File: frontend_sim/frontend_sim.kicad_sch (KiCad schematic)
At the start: 15 parts, among them U1 TL072

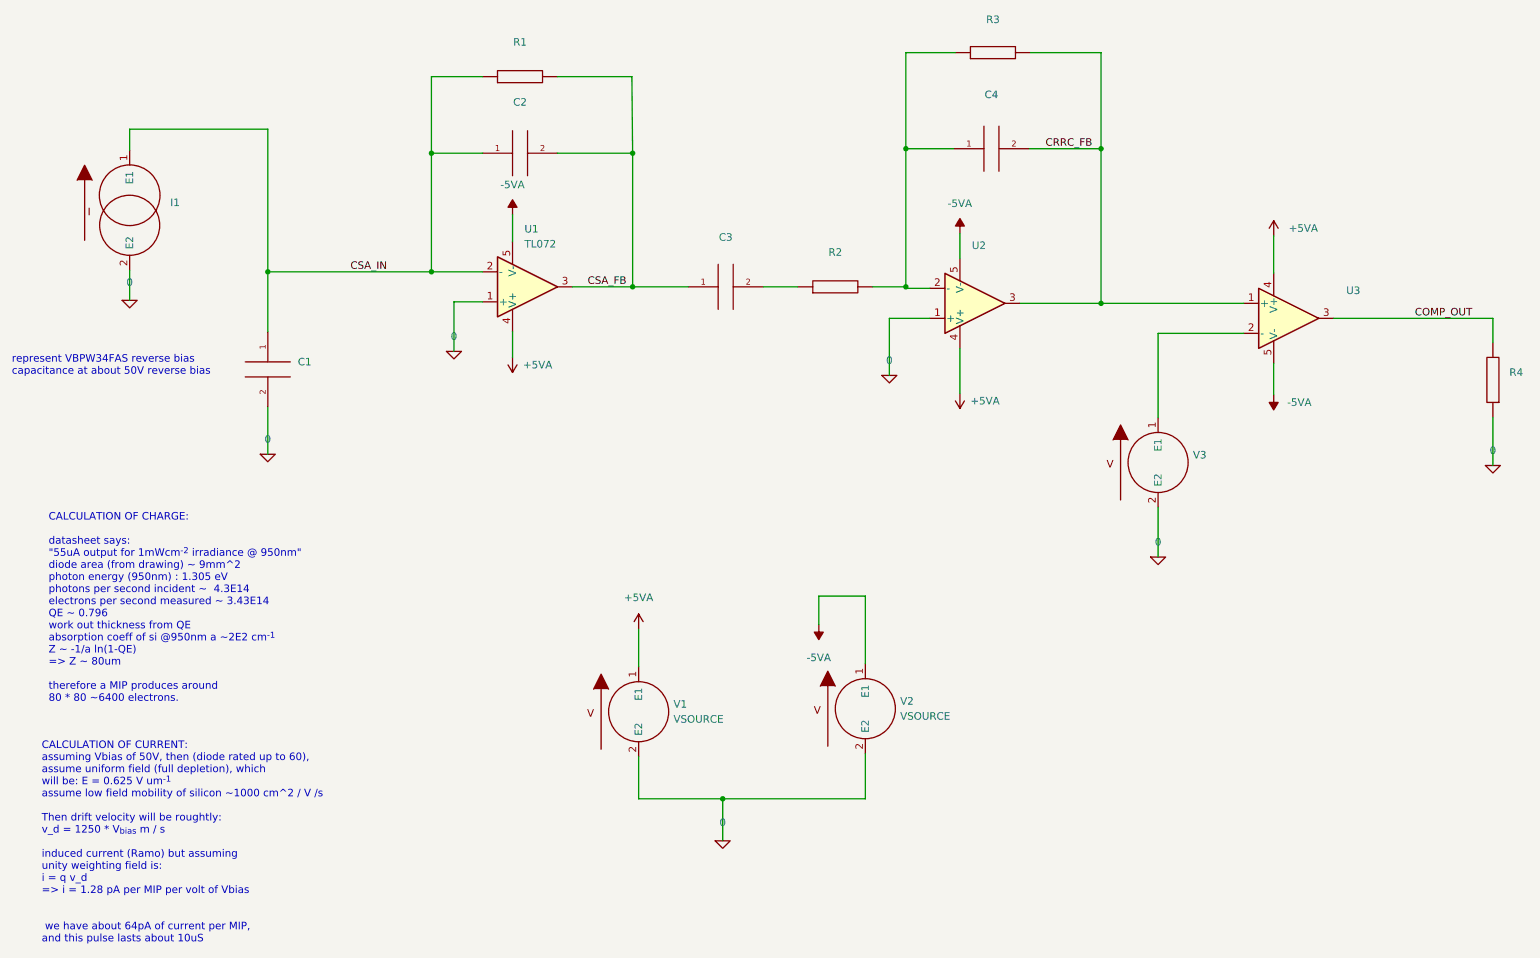
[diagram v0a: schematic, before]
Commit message: frontend sim update to v8, working at least AC scan mode
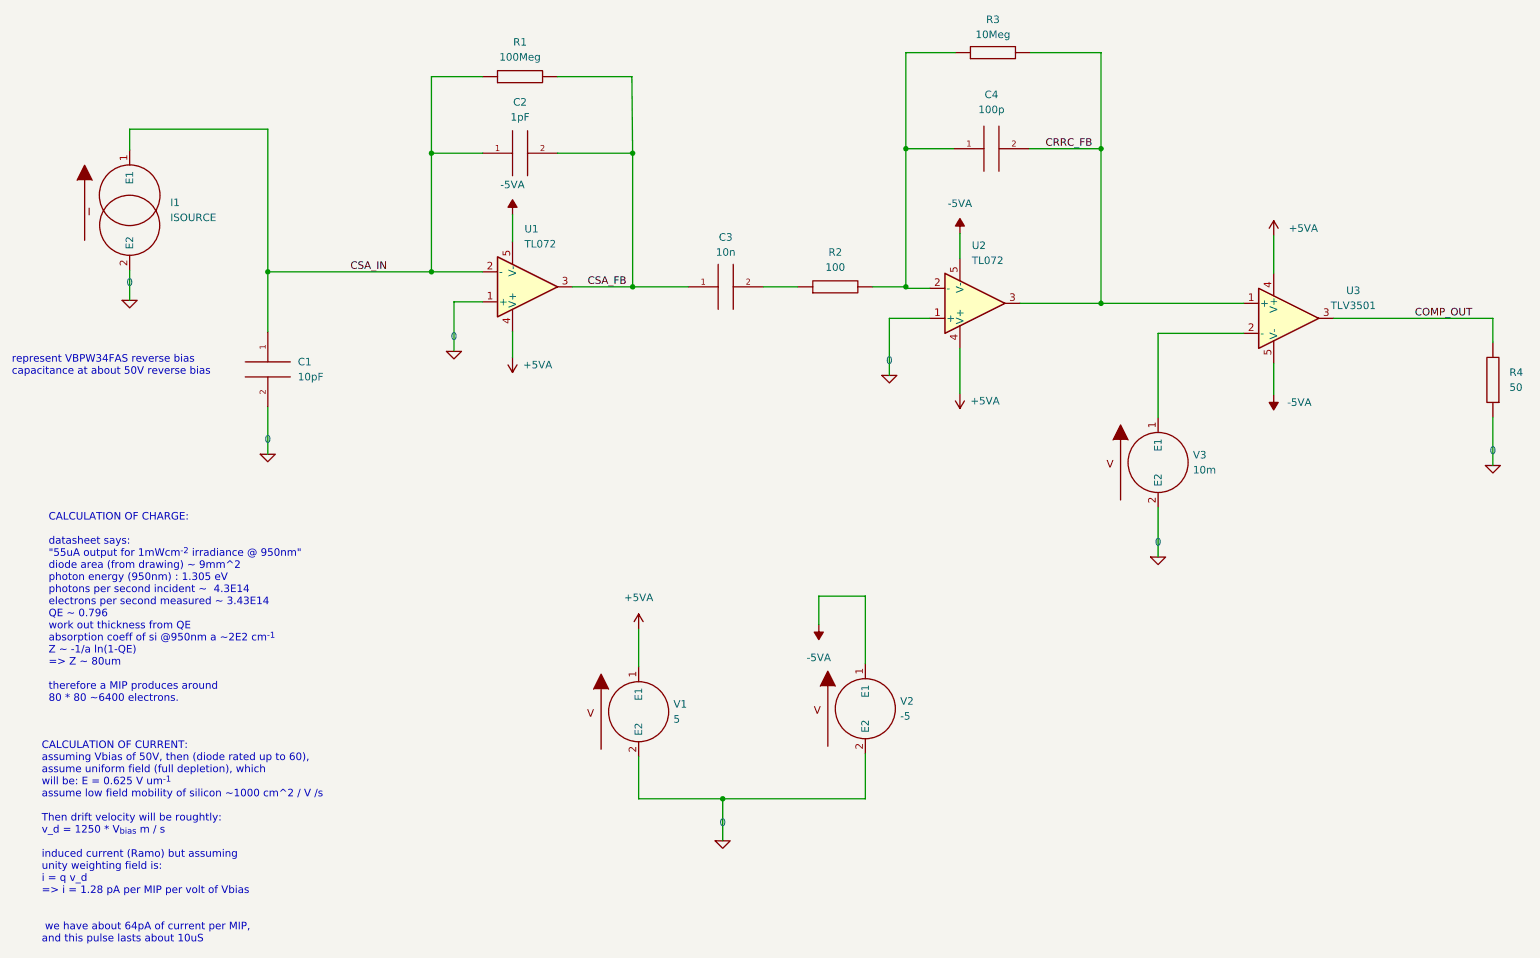
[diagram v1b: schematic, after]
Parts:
- C1: value (none) -> 10pF
- C2: value (none) -> 1pF; Spice_Model 2p -> (none); Spice_Netlist_Enabled Y -> (none); Spice_Primitive C -> (none)
- C3: value (none) -> 10n; Spice_Model 10n -> (none); Spice_Netlist_Enabled Y -> (none); Spice_Primitive C -> (none)
- C4: value (none) -> 100p; Spice_Model 10p -> (none); Spice_Netlist_Enabled Y -> (none); Spice_Primitive C -> (none)
- I1: value (none) -> ISOURCE; Spice_Model dc 0 ac 10n pulse(0 -100p 1n 100p 100p 1u) -> (none); Spice_Netlist_Enabled Y -> (none); Spice_Primitive I -> (none)
- R1: value (none) -> 100Meg; Spice_Model 100Meg -> (none); Spice_Netlist_Enabled Y -> (none); Spice_Primitive R -> (none)
- R2: value (none) -> 100; Spice_Model 100 -> (none); Spice_Netlist_Enabled Y -> (none); Spice_Primitive R -> (none)
- R3: value (none) -> 10Meg; Spice_Model 100Meg -> (none); Spice_Netlist_Enabled Y -> (none); Spice_Primitive R -> (none)
- R4: value (none) -> 50; Spice_Model 50 -> (none); Spice_Netlist_Enabled Y -> (none); Spice_Primitive R -> (none)
- U1: Spice_Lib_File TL072.301 -> (none); Spice_Model TL072 -> (none); Spice_Netlist_Enabled Y -> (none); Spice_Node_Sequence 1 2 4 5 3 -> (none); Spice_Primitive X -> (none)
- U2: value (none) -> TL072; Spice_Lib_File TL072.301 -> (none); Spice_Model TL072 -> (none); Spice_Netlist_Enabled Y -> (none); Spice_Node_Sequence 1 2 4 5 3 -> (none); Spice_Primitive X -> (none)
- U3: value (none) -> TLV3501; Spice_Lib_File tlv3501.lib -> (none); Spice_Model TLV3501 -> (none); Spice_Netlist_Enabled Y -> (none); Spice_Node_Sequence 1 2 4 4 5 3 -> (none); Spice_Primitive X -> (none)
- V1: value VSOURCE -> 5; Spice_Model dc 5 -> (none); Spice_Netlist_Enabled Y -> (none); Spice_Primitive V -> (none)
- V2: value VSOURCE -> -5; Spice_Model dc -5 -> (none); Spice_Netlist_Enabled Y -> (none); Spice_Primitive V -> (none)
- V3: value (none) -> 10m; Spice_Model dc 10m -> (none); Spice_Netlist_Enabled Y -> (none); Spice_Primitive V -> (none)
